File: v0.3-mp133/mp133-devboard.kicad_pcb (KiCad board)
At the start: 4 copper layers, 39.9 x 57.9 mm, 122 parts, among them CON1 microSDCon_SMT_104031-0811, J1 Pins_02x40_P0.4mm_W3.0mm_SMT, J2 Pins_02x40_P0.4mm_W3.0mm_SMT, J3 USB-C_Receptacle_Molex_217179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, J4 Pins_02x04_RightAngle_P2.54mm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, J5 Conn_01x02, J6 Pins_02x05_P1.27mm_SMT, U13 NCP51460SN33, U14 DDR3L-RAM-4Gb_MT41K256M16TW, U15 AP6230xZ6, U16 AP6230xZ6, U17 AP6230xZ6, U18 TAR5S33, U19 TAR5S33, U2 STM32MP15xxAD, U20 AP2411SN, U3 USBLC6-2SC6, U5 NORFLASH_W25Q128JV, X1 24MHz_8pF_2x1.6mm

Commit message: Work on mp133 devboard PCB
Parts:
- removed C50, C51, C52, C53, C54, C55, C59, C60, C62, C63, C70, C73, C79: 1uF_0402_25V, 4ms_Capacitor:C_0402
- removed C61, C64, C82, C87, C93, C95: 100nF_0402_16V, 4ms_Capacitor:C_0402
- removed C71, C74, C80: 3.3nF_0402_16V, 4ms_Capacitor:C_0402
- removed R41: 10k_0402, 4ms_Resistor:R_0402
- removed X1: 24MHz_8pF_2x1.6mm, 4ms_Crystal:Crystal_2.0x1.6mm_4pin
- added C102: 100nF_0402_16V, 4ms_Capacitor:C_0402, B.Cu at (254.1, 59.8)
- added C103: 100nF_0402_16V, 4ms_Capacitor:C_0402, B.Cu at (243.6, 65.3)
- added C106: 100nF_0402_16V, 4ms_Capacitor:C_0402, B.Cu at (244.0, 55.9)
- added C110: 6.8pF_0402_25V, 4ms_Capacitor:C_0402, F.Cu at (251.5, 85.8)
- added C110: 6.8pF_0402_25V, 4ms_Capacitor:C_0402, F.Cu at (142.8, 74.5)
- added C111: 6.8pF_0402_25V, 4ms_Capacitor:C_0402, F.Cu at (142.8, 76.5)
- added C111: 6.8pF_0402_25V, 4ms_Capacitor:C_0402, F.Cu at (253.6, 84.1)
- added C13: 1uF_0402_25V, 4ms_Capacitor:C_0402, B.Cu at (250.9, 72.1)
- added C174: 1uF_0201_4V, 4ms_Capacitor:C_0201, F.Cu at (142.5, 64.2)
- added C174: 1uF_0201_4V, 4ms_Capacitor:C_0201, B.Cu at (245.1, 79.1)
- added C175: 1nF_0201_4V, 4ms_Capacitor:C_0201, F.Cu at (142.5, 65.9)
- added C175: 1nF_0201_4V, 4ms_Capacitor:C_0201, B.Cu at (245.1, 74.7)
- added C176: 1uF_0201_4V, 4ms_Capacitor:C_0201, F.Cu at (142.5, 67.6)
- added C176: 1uF_0201_4V, 4ms_Capacitor:C_0201, B.Cu at (245.2, 76.5)
- added C177: 1uF_0201_4V, 4ms_Capacitor:C_0201, F.Cu at (142.5, 69.3)
- added C177: 1uF_0201_4V, 4ms_Capacitor:C_0201, B.Cu at (245.2, 77.7)
- added C182: 1uF_0201_4V, 4ms_Capacitor:C_0201, F.Cu at (142.5, 71.0)
- added C182: 1uF_0201_4V, 4ms_Capacitor:C_0201, B.Cu at (249.3, 55.0)
- added C183: 1uF_0201_4V, 4ms_Capacitor:C_0201, F.Cu at (142.5, 72.6)
- added C183: 1uF_0201_4V, 4ms_Capacitor:C_0201, B.Cu at (246.1, 80.0)
- added C184: 1nF_0201_4V, 4ms_Capacitor:C_0201, F.Cu at (144.7, 64.2)
- added C184: 1nF_0201_4V, 4ms_Capacitor:C_0201, B.Cu at (246.2, 74.9)
- added C185: 1uF_0201_4V, 4ms_Capacitor:C_0201, F.Cu at (144.7, 65.9)
- added C185: 1uF_0201_4V, 4ms_Capacitor:C_0201, B.Cu at (246.2, 76.1)
- added C186: 1uF_0201_4V, 4ms_Capacitor:C_0201, F.Cu at (144.7, 67.6)
- added C186: 1uF_0201_4V, 4ms_Capacitor:C_0201, B.Cu at (246.2, 77.6)
- added C187: 1uF_0201_4V, 4ms_Capacitor:C_0201, F.Cu at (144.7, 69.3)
- added C187: 1uF_0201_4V, 4ms_Capacitor:C_0201, B.Cu at (246.2, 78.8)
- added C188: 1uF_0201_4V, 4ms_Capacitor:C_0201, F.Cu at (144.7, 71.0)
- added C188: 1uF_0201_4V, 4ms_Capacitor:C_0201, B.Cu at (247.3, 75.8)
- added C189: 1uF_0201_4V, 4ms_Capacitor:C_0201, F.Cu at (144.7, 72.6)
- added C189: 1uF_0201_4V, 4ms_Capacitor:C_0201, B.Cu at (247.2, 76.8)
- added C190: 1uF_0201_4V, 4ms_Capacitor:C_0201, F.Cu at (147.0, 64.2)
- added C190: 1uF_0201_4V, 4ms_Capacitor:C_0201, B.Cu at (247.3, 77.9)
- added C191: 1uF_0201_4V, 4ms_Capacitor:C_0201, F.Cu at (147.0, 65.9)
- added C191: 1uF_0201_4V, 4ms_Capacitor:C_0201, B.Cu at (247.6, 80.0)
- added C192: 1nF_0201_4V, 4ms_Capacitor:C_0201, F.Cu at (147.0, 67.6)
- added C192: 1nF_0201_4V, 4ms_Capacitor:C_0201, B.Cu at (247.6, 56.9)
- added C193: 1nF_0201_4V, 4ms_Capacitor:C_0201, F.Cu at (147.0, 69.3)
- added C193: 1nF_0201_4V, 4ms_Capacitor:C_0201, B.Cu at (247.7, 74.9)
- added C194: 1uF_0201_4V, 4ms_Capacitor:C_0201, F.Cu at (147.0, 71.0)
- added C194: 1uF_0201_4V, 4ms_Capacitor:C_0201, B.Cu at (247.7, 78.9)
- added C195: 1uF_0201_4V, 4ms_Capacitor:C_0201, F.Cu at (147.0, 72.6)
- added C195: 1uF_0201_4V, 4ms_Capacitor:C_0201, B.Cu at (248.2, 76.1)
- added C196: 1uF_0201_4V, 4ms_Capacitor:C_0201, F.Cu at (149.2, 64.2)
- added C196: 1uF_0201_4V, 4ms_Capacitor:C_0201, B.Cu at (248.2, 77.6)
- added C197: 1uF_0201_4V, 4ms_Capacitor:C_0201, F.Cu at (149.2, 65.9)
- added C197: 1uF_0201_4V, 4ms_Capacitor:C_0201, B.Cu at (248.9, 80.0)
- added C198: 1uF_0201_4V, 4ms_Capacitor:C_0201, F.Cu at (149.2, 67.6)
- added C198: 1uF_0201_4V, 4ms_Capacitor:C_0201, B.Cu at (250.2, 74.8)
- added C199: 1uF_0201_4V, 4ms_Capacitor:C_0201, F.Cu at (149.2, 69.3)
- added C199: 1uF_0201_4V, 4ms_Capacitor:C_0201, B.Cu at (249.0, 74.9)
- added C200: 1uF_0201_4V, 4ms_Capacitor:C_0201, F.Cu at (149.2, 71.0)
- added C200: 1uF_0201_4V, 4ms_Capacitor:C_0201, B.Cu at (249.2, 75.9)
- added C201: 1uF_0201_4V, 4ms_Capacitor:C_0201, F.Cu at (149.2, 72.6)
- added C201: 1uF_0201_4V, 4ms_Capacitor:C_0201, B.Cu at (248.9, 78.9)
- added C202: 1uF_0201_4V, 4ms_Capacitor:C_0201, F.Cu at (151.5, 64.2)
- added C202: 1uF_0201_4V, 4ms_Capacitor:C_0201, B.Cu at (249.2, 77.9)
- added C203: 1uF_0201_4V, 4ms_Capacitor:C_0201, F.Cu at (151.5, 65.9)
- added C203: 1uF_0201_4V, 4ms_Capacitor:C_0201, B.Cu at (249.1, 77.0)
- added C204: 1nF_0201_4V, 4ms_Capacitor:C_0201, F.Cu at (151.5, 67.6)
- added C204: 1nF_0201_4V, 4ms_Capacitor:C_0201, B.Cu at (250.3, 73.9)
- added C205: 1uF_0201_4V, 4ms_Capacitor:C_0201, F.Cu at (151.5, 69.3)
- added C205: 1uF_0201_4V, 4ms_Capacitor:C_0201, B.Cu at (250.1, 78.8)
- added C206: 1nF_0201_4V, 4ms_Capacitor:C_0201, F.Cu at (151.5, 71.0)
- added C206: 1nF_0201_4V, 4ms_Capacitor:C_0201, B.Cu at (248.5, 73.9)
- added C207: 1uF_0201_4V, 4ms_Capacitor:C_0201, F.Cu at (151.5, 72.6)
- added C207: 1uF_0201_4V, 4ms_Capacitor:C_0201, B.Cu at (250.4, 79.9)
- added C208: 1uF_0201_4V, 4ms_Capacitor:C_0201, F.Cu at (153.7, 64.2)
- added C208: 1uF_0201_4V, 4ms_Capacitor:C_0201, B.Cu at (250.3, 76.6)
- added C209: 1uF_0201_4V, 4ms_Capacitor:C_0201, F.Cu at (153.7, 65.9)
- added C209: 1uF_0201_4V, 4ms_Capacitor:C_0201, B.Cu at (250.3, 77.8)
- added C211: 1nF_0201_4V, 4ms_Capacitor:C_0201, F.Cu at (153.7, 67.6)
- added C211: 1nF_0201_4V, 4ms_Capacitor:C_0201, B.Cu at (251.2, 74.2)
- added C212: 1uF_0201_4V, 4ms_Capacitor:C_0201, F.Cu at (153.7, 69.3)
- added C212: 1uF_0201_4V, 4ms_Capacitor:C_0201, B.Cu at (251.2, 75.5)
- added C213: 1uF_0201_4V, 4ms_Capacitor:C_0201, F.Cu at (153.7, 71.0)
- added C213: 1uF_0201_4V, 4ms_Capacitor:C_0201, B.Cu at (251.2, 76.7)
- added C215: 1uF_0201_4V, 4ms_Capacitor:C_0201, F.Cu at (153.7, 72.6)
- added C215: 1uF_0201_4V, 4ms_Capacitor:C_0201, B.Cu at (251.4, 79.3)
- added C29: 2.2uF_0402_6.3V, 4ms_Capacitor:C_0402, B.Cu at (252.5, 76.7)
- added C30: 100nF_0402_16V, 4ms_Capacitor:C_0402, B.Cu at (253.0, 79.9)
- added C31: 1uF_0402_25V, 4ms_Capacitor:C_0402, B.Cu at (252.9, 78.9)
- added C32: 2.2uF_0402_6.3V, 4ms_Capacitor:C_0402, B.Cu at (254.2, 75.3)
- added C33: 1uF_0402_25V, 4ms_Capacitor:C_0402, B.Cu at (252.4, 81.0)
- added C42: 100nF_0402_16V, 4ms_Capacitor:C_0402, B.Cu at (253.4, 64.2)
- added C43: 100nF_0402_16V, 4ms_Capacitor:C_0402, B.Cu at (243.6, 60.1)
- added C72: 100nF_0402_50V, 4ms_Capacitor:C_0402, B.Cu at (254.6, 81.9)
- added C81: 10uF_0603_10V, 4ms_Capacitor:C_0603, F.Cu at (254.2, 56.8)
- added C83: 10uF_0603_10V, 4ms_Capacitor:C_0603, B.Cu at (242.7, 55.8)
- added C84: 4.7uF_0402_6.3V, 4ms_Capacitor:C_0402, B.Cu at (254.6, 79.8)
- added C92: 100nF_0402_16V, 4ms_Capacitor:C_0402, B.Cu at (243.6, 59.1)
- added C94: 100nF_0402_16V, 4ms_Capacitor:C_0402, B.Cu at (251.6, 57.4)
- added C98: 100nF_0402_16V, 4ms_Capacitor:C_0402, F.Cu at (253.9, 66.5)
- added C99: 100nF_0402_16V, 4ms_Capacitor:C_0402, F.Cu at (255.5, 56.9)
- added D11: BAT54LP, 4ms_Diode:DFN-1006-2, F.Cu at (256.1, 72.9)
- added D26: BAT54LP, 4ms_Diode:DFN-1006-2, F.Cu at (255.7, 71.5)
- added D26: BAT54LP, 4ms_Diode:DFN-1006-2, F.Cu at (145.8, 78.3)
- added L4: 1uH_3.2A_2520, Inductor_SMD:L_1008_2520Metric, F.Cu at (146.7, 75.4)
- added R30: 10k_0402, 4ms_Resistor:R_0402, B.Cu at (250.9, 84.9)
- added R52: 240Ω_0402, 4ms_Resistor:R_0402, B.Cu at (253.9, 73.7)
- added R59: 240Ω_0402, 4ms_Resistor:R_0402, B.Cu at (253.4, 63.0)
- added R67: 10k_0402, 4ms_Resistor:R_0402, B.Cu at (253.4, 62.0)
- added R68: 100Ω_0402, 4ms_Resistor:R_0402, B.Cu at (249.6, 61.4)
- added R69: 10k_0402, 4ms_Resistor:R_0402, B.Cu at (242.8, 73.9)
- added R76: 10k_0402, 4ms_Resistor:R_0402, F.Cu at (139.9, 64.3)
- added R76: 10k_0402, 4ms_Resistor:R_0402, F.Cu at (255.1, 73.0)
- added R77: 10k_0402, 4ms_Resistor:R_0402, F.Cu at (254.8, 70.0)
- added R77: 10k_0402, 4ms_Resistor:R_0402, F.Cu at (139.9, 66.3)
- added R78: 1k_0402, 4ms_Resistor:R_0402, F.Cu at (139.9, 68.3)
- added R78: 1k_0402, 4ms_Resistor:R_0402, B.Cu at (252.8, 72.1)
- added R79: 1k_0402, 4ms_Resistor:R_0402, F.Cu at (139.9, 70.3)
- added R79: 1k_0402, 4ms_Resistor:R_0402, B.Cu at (251.9, 72.1)
- added R80: 10k_0402, 4ms_Resistor:R_0402, F.Cu at (139.9, 72.3)
- added R81: 14.7k_0402, 4ms_Resistor:R_0402, F.Cu at (139.9, 74.3)
- added U14: DDR3L-RAM-4Gb_MT41K256M16TW, 4ms_Package_QFP:FBGA-96_Layout2x3x16_Body8x14_P0.8mm, F.Cu at (248.4, 61.5)
- added U2: STM32MP131DAF7, 4ms_Package_QFP:TFBGA-320_11x11mm_P0.5, F.Cu at (248.2, 76.9)
- added U21: AP6230xZ6, 4ms_Package_SOT:SOT-563, F.Cu at (151.2, 78.5)
- added X2: 24MHz_8pF_2x1.6mm, 4ms_Crystal:Crystal_2.0x1.6mm_4pin, F.Cu at (151.2, 75.1)
- added X2: 24MHz_8pF_2x1.6mm, 4ms_Crystal:Crystal_2.0x1.6mm_4pin, F.Cu at (251.8, 84.2)
- C13: value 6.8pF_0402_25V -> 1uF_0402_25V
- C14: value 6.8pF_0402_25V -> 2.2uF_0603_25V; footprint 4ms_Capacitor:C_0402 -> 4ms_Capacitor:C_0603
- C24: value 10nF_0402_16V -> 100nF_0402_16V
- C40: value 100nF_0402_16V -> 22uF_0603_6.3V; footprint 4ms_Capacitor:C_0402 -> 4ms_Capacitor:C_0603
- R62: value 20k_0402 -> 17.4k_0402
- U2: value STM32MP15xxAD -> STM32MP133DAF
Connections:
- C13 pad 2: Net-(U2B-PH0-OSC_IN) -> VREF_DDR
- C14 pad 2: Net-(U2B-PH1-OSC_OUT) -> +12V
- C24 pad 1: GND -> Net-(U21-SW)
- C24 pad 2: /NRST_CORE -> Net-(U21-BST)
- C29 pad 2: Net-(U2D-VDDA1V1_REG) -> Net-(U2E-VDDA1V1_REG)
- C40 pad 2: VREF_DDR -> VDD_CPU
- J1 pad 1: /PD3 -> Net-(J1-Pin_1)
- J1 pad 11: /PE4 -> /PB9
- J1 pad 12: /PE4 -> /PB9
- J1 pad 2: /PD3 -> Net-(J1-Pin_1)
- J1 pad 3: /PA8 -> Net-(J1-Pin_3)
- J1 pad 39: /PC7 -> Net-(J1-Pin_39)
- J1 pad 4: /PA8 -> Net-(J1-Pin_3)
- J1 pad 40: /PC7 -> Net-(J1-Pin_39)
- J1 pad 41: /PA10 -> Net-(J1-Pin_41)
- J1 pad 42: /PA10 -> Net-(J1-Pin_41)
- J1 pad 43: /PE0 -> /PD0
- J1 pad 44: /PE0 -> /PD0
- J1 pad 45: /PD12 -> /PE11
- J1 pad 46: /PD12 -> /PE11
- J1 pad 47: /PD13 -> /PH12
- J1 pad 48: /PD13 -> /PH12
- J1 pad 49: /PD11 -> /PD6
- J1 pad 5: /PB9 -> Net-(J1-Pin_5)
- J1 pad 50: /PD11 -> /PD6
- J1 pad 55: /PB10 -> Net-(J1-Pin_55)
- J1 pad 56: /PB10 -> Net-(J1-Pin_55)
- J1 pad 57: /PG9 -> Net-(J1-Pin_57)
- J1 pad 58: /PG9 -> Net-(J1-Pin_57)
- J1 pad 59: /PA12 -> /PE8
- J1 pad 6: /PB9 -> Net-(J1-Pin_5)
- J1 pad 60: /PA12 -> /PE8
- J1 pad 61: /PA11 -> /PD12
- J1 pad 62: /PA11 -> /PD12
- J1 pad 63: /PE10 -> Net-(J1-Pin_63)
- J1 pad 64: /PE10 -> Net-(J1-Pin_63)
- J2 pad 1: /PE3 -> Net-(J2-Pin_1)
- J2 pad 10: /PB7 -> /PD7
- J2 pad 11: /PE11 -> /PH11
- J2 pad 12: /PE11 -> /PH11
- J2 pad 13: /PC6 -> Net-(J2-Pin_13)
- J2 pad 14: /PC6 -> Net-(J2-Pin_13)
- J2 pad 15: /PE6 -> /PA8
- J2 pad 16: /PE6 -> /PA8
- J2 pad 17: /PG15 -> Net-(J2-Pin_17)
- J2 pad 18: /PG15 -> Net-(J2-Pin_17)
- J2 pad 19: /PE12 -> /PH6
- J2 pad 2: /PE3 -> Net-(J2-Pin_1)
- J2 pad 20: /PE12 -> /PH6
- J2 pad 21: /PE13 -> /PG1
- J2 pad 22: /PE13 -> /PG1
- J2 pad 3: /PD10 -> Net-(J2-Pin_3)
- J2 pad 31: /PA3 -> /PA1
- J2 pad 32: /PA3 -> /PA1
- J2 pad 33: /PC3 -> /PA2
- J2 pad 34: /PC3 -> /PA2
- J2 pad 35: /PC2 -> Net-(J2-Pin_35)
- J2 pad 36: /PC2 -> Net-(J2-Pin_35)
- J2 pad 37: /PC1 -> /PA4
- J2 pad 38: /PC1 -> /PA4
- J2 pad 39: /PA1 -> /PA5
- J2 pad 4: /PD10 -> Net-(J2-Pin_3)
- J2 pad 40: /PA1 -> /PA5
- J2 pad 41: /PB0 -> /PC0
- J2 pad 42: /PB0 -> /PC0
- J2 pad 43: /PA2 -> /PA7
- J2 pad 44: /PA2 -> /PA7
- J2 pad 45: /PB1 -> /PC1
- J2 pad 46: /PB1 -> /PC1
- J2 pad 47: /PC5 -> /PC2
- J2 pad 48: /PC5 -> /PC2
- J2 pad 5: /PB4 -> Net-(J2-Pin_5)
- J2 pad 51: /PC0 -> /PC5
- J2 pad 52: /PC0 -> /PC5
- J2 pad 53: /PA7 -> /PA3
- J2 pad 54: /PA7 -> /PA3
- J2 pad 55: /PA5 -> /PC3
- J2 pad 56: /PA5 -> /PC3
- J2 pad 59: /PA4 -> /PF12
- J2 pad 6: /PB4 -> Net-(J2-Pin_5)
- J2 pad 60: /PA4 -> /PF12
- J2 pad 61: /PF11 -> /PB0
- J2 pad 62: /PF11 -> /PB0
- J2 pad 69: /PE2 -> Net-(J2-Pin_69)
- J2 pad 7: /PG6 -> Net-(J2-Pin_7)
- J2 pad 70: /PE2 -> Net-(J2-Pin_69)
- J2 pad 71: /PG13 -> Net-(J2-Pin_71)
- J2 pad 72: /PG13 -> Net-(J2-Pin_71)
- J2 pad 73: /PB8 -> /PH3
- J2 pad 74: /PB8 -> /PH3
- J2 pad 75: /PB2 -> Net-(J2-Pin_75)
- J2 pad 76: /PB2 -> Net-(J2-Pin_75)
- J2 pad 8: /PG6 -> Net-(J2-Pin_7)
- J2 pad 9: /PB7 -> /PD7
- JP2 pad 1: /PB14 -> /DEBUG3
- JP3 pad 3: /PB15 -> /DEBUG2
- R52 pad 1: Net-(U2E-DDR_ZQ) -> Net-(U2C-DDR_ZQ)
- U14 pad A2: /DDR_DQ7 -> /DDR_DQ5
- U14 pad A7: /DDR_DQ2 -> /DDR_DQ0
- U14 pad B8: /DDR_DQ4 -> /DDR_DQ1
- U14 pad C2: /DDR_DQ1 -> /DDR_DQ6
- U14 pad C3: /DDR_DQ0 -> /DDR_DQ7
- U14 pad C8: /DDR_DQ5 -> /DDR_DQ4
- U14 pad D7: /DDR_DQ6 -> /DDR_DQ2
- U14 pad E3: /DDR_DQ9 -> /DDR_DQ8
- U14 pad F2: /DDR_DQ8 -> /DDR_DQ13
- U14 pad F7: /DDR_DQ11 -> /DDR_DQ15
- U14 pad F8: /DDR_DQ15 -> /DDR_DQ12
- U14 pad H3: /DDR_DQ13 -> /DDR_DQ9
- U14 pad H8: /DDR_DQ12 -> /DDR_DQ11
- U2 pad 1A1: unconnected-(U2B-PE1-Pad1A1) -> (no net)
- U2 pad 1A2: /PD10 -> (no net)
- U2 pad 1A3: /PE3 -> (no net)
- U2 pad 1A4: /PB14 -> (no net)
- U2 pad 1A5: /PD2 -> (no net)
- U2 pad 1A6: GND -> (no net)
- U2 pad 1A7: unconnected-(U2D-VDD1V2_DSI_REG-Pad1A7) -> (no net)
- U2 pad 1A8: Net-(U2E-DDR_ZQ) -> (no net)
- U2 pad 1A9: /DDR_A7 -> (no net)
- U2 pad 1B1: unconnected-(U2A-PD6-Pad1B1) -> (no net)
- U2 pad 1B2: unconnected-(U2B-PE14-Pad1B2) -> (no net)
- U2 pad 1B3: VDD_CORE -> (no net)
- U2 pad 1B4: /PC12 -> (no net)
- U2 pad 1B5: VDD_CORE -> (no net)
- U2 pad 1B6: unconnected-(U2D-VDDA1V8_DSI-Pad1B6) -> (no net)
- U2 pad 1B7: unconnected-(U2D-VDD1V2_DSI_PHY-Pad1B7) -> (no net)
- U2 pad 1B8: GND -> (no net)
- U2 pad 1B9: VDD_DDR -> (no net)
- U2 pad 1C1: unconnected-(U2A-PD9-Pad1C1) -> (no net)
- U2 pad 1C2: unconnected-(U2A-PD15-Pad1C2) -> (no net)
- U2 pad 1C3: GND -> (no net)
- U2 pad 1C4: VDD_CORE -> (no net)
- U2 pad 1C5: GND -> (no net)
- U2 pad 1C6: VDD_CORE -> (no net)
- U2 pad 1C7: GND -> (no net)
- U2 pad 1C8: unconnected-(U2E-DDR_DTO1-Pad1C8) -> (no net)
- U2 pad 1C9: /DDR_A5 -> (no net)
- U2 pad 1D1: VDD -> (no net)
- U2 pad 1D2: GND -> (no net)
- U2 pad 1D3: VDD_CORE -> (no net)
- U2 pad 1D4: GND -> (no net)
- U2 pad 1D5: VDD_CORE -> (no net)
- U2 pad 1D6: GND -> (no net)
- U2 pad 1D7: VDD_CORE -> (no net)
- U2 pad 1D8: unconnected-(U2E-DDR_DTO0-Pad1D8) -> (no net)
- U2 pad 1D9: VDD_DDR -> (no net)
- U2 pad 1E1: unconnected-(U2A-PD14-Pad1E1) -> (no net)
- U2 pad 1E2: VDD -> (no net)
- U2 pad 1E3: GND -> (no net)
- U2 pad 1E4: VDD_CORE -> (no net)
- U2 pad 1E5: GND -> (no net)
- U2 pad 1E6: VDD_CORE -> (no net)
- U2 pad 1E7: GND -> (no net)
- U2 pad 1E8: VDD_CORE -> (no net)
- U2 pad 1E9: /DDR_RASN -> (no net)
- U2 pad 1F1: VDDA -> (no net)
- U2 pad 1F2: VDDA -> (no net)
- U2 pad 1F3: VDD -> (no net)
- U2 pad 1F4: GND -> (no net)
- U2 pad 1F5: VDD_CORE -> (no net)
- U2 pad 1F6: GND -> (no net)
- U2 pad 1F7: VDD_CORE -> (no net)
- U2 pad 1F8: unconnected-(U2E-DDR_ATO-Pad1F8) -> (no net)
- U2 pad 1F9: VDD_DDR -> (no net)
- U2 pad 1G1: GNDADC -> (no net)
- U2 pad 1G2: GND -> (no net)
- U2 pad 1G3: VDD -> (no net)
- U2 pad 1G4: VDD -> (no net)
- U2 pad 1G5: GND -> (no net)
- U2 pad 1G6: VDD_CORE -> (no net)
- U2 pad 1G7: GND -> (no net)
- U2 pad 1G8: VDD_CORE -> (no net)
- U2 pad 1G9: /DDR_A6 -> (no net)
- U2 pad 1H1: /PA5 -> (no net)
- U2 pad 1H2: GND -> (no net)
- U2 pad 1H3: GND -> (no net)
- U2 pad 1H4: GND -> (no net)
- U2 pad 1H5: VDDA_1V8 -> (no net)
- U2 pad 1H6: GND -> (no net)
- U2 pad 1H7: VDD_USB -> (no net)
- U2 pad 1H8: GND -> (no net)
- U2 pad 1H9: VDD_DDR -> (no net)
- U2 pad 1J1: /PA4 -> (no net)
- U2 pad 1J2: unconnected-(U2A-PB13-Pad1J2) -> (no net)
- U2 pad 1J3: VDD -> (no net)
- U2 pad 1J4: unconnected-(U2B-PE9-Pad1J4) -> (no net)
- U2 pad 1J5: GND -> (no net)
- U2 pad 1J6: Net-(U2D-VDDA1V1_REG) -> (no net)
- U2 pad 1J7: /FLASH_CLK -> (no net)
- U2 pad 1J8: /USB_RREF -> (no net)
- U2 pad 1J9: GND -> (no net)
- U2 pad A10: /PE4 -> unconnected-(U2B-PG7-PadA10)
- U2 pad A15: /JTDO_SWO -> /PB9
- U2 pad A16: /JTCK_SWCLK -> unconnected-(U2B-PF0-PadA16)
- U2 pad A17: /DDR_DQ0 -> (no net)
- U2 pad A18: /DDR_DQ1 -> /PC10
- U2 pad A19: GND -> /PC12
- U2 pad A3: /PB7 -> /PE13
- U2 pad A4: /PC6 -> /PE12
- U2 pad A6: GND -> /PD12
- U2 pad A7: /PD3 -> /PG0
- U2 pad A9: /PC8 -> unconnected-(U2B-PE15-PadA9)
- U2 pad B1: /PG15 -> /PD0
- U2 pad B10: /PC10 -> /PG4
- U2 pad B12: unconnected-(U2C-DSI_CKN-PadB12) -> GND
- U2 pad B14: /JTRST -> /PC6
- U2 pad B15: /JTDI -> unconnected-(U2A-PB15-PadB15)
- U2 pad B16: /DDR_DQ3 -> unconnected-(U2A-PB14-PadB16)
- U2 pad B17: /DDR_DQ7 -> /PE3
- U2 pad B18: /DDR_DQS0_N -> /PC11
- U2 pad B19: /DDR_DQS0_P -> /DDR_DQ4
- U2 pad B2: /PE6 -> /PE11
- U2 pad B3: /DEBUG0 -> unconnected-(U2B-PF5-PadB3)
- U2 pad B4: unconnected-(U2A-PA15-PadB4) -> /UART_RX
- U2 pad B5: /PG6 -> unconnected-(U2A-PD8-PadB5)
- U2 pad B6: /PB4 -> /PE0
- U2 pad B7: /DEBUG1 -> unconnected-(U2B-PE9-PadB7)
- U2 pad B8: /PA8 -> unconnected-(U2B-PH14-PadB8)
- U2 pad B9: /PC9 -> /PE8
- U2 pad C1: /PE12 -> unconnected-(U2A-PB6-PadC1)
- U2 pad C10: /PC7 -> /PE10
- U2 pad C11: /PC11 -> unconnected-(U2A-PB12-PadC11)
- U2 pad C13: unconnected-(U2D-VDD_DSI-PadC13) -> /PC7
- U2 pad C14: GND -> /DEBUG0
- U2 pad C15: /JTMS_SWDIO -> VDD
- U2 pad C16: /DDR_RESETN -> /DEBUG1
- U2 pad C17: /DDR_DQM0 -> /PG6
- U2 pad C18: /DDR_DQ2 -> /PC8
- U2 pad C19: /DDR_DQ6 -> /PD2
- U2 pad C2: /PE0 -> /PD3
- U2 pad C5: /UART_RX -> unconnected-(U2A-PD1-PadC5)
- U2 pad C6: unconnected-(U2A-PA9-PadC6) -> /PB7
- U2 pad C8: /PB15 -> unconnected-(U2A-PD5-PadC8)
- U2 pad C9: /PB9 -> unconnected-(U2A-PD9-PadC9)
- U2 pad D1: unconnected-(U2B-PG12-PadD1) -> /PB8
- U2 pad D17: GND -> (no net)
- U2 pad D18: /DDR_DQ4 -> (no net)
- U2 pad D19: /DDR_DQ5 -> /DDR_DQ2
- U2 pad D2: /PE11 -> /PD6
- U2 pad D3: unconnected-(U2B-PE15-PadD3) -> /PH12
- U2 pad E1: /DFU_BOOT -> (no net)
- U2 pad E17: /DDR_A13 -> VDD
- U2 pad E18: /DDR_A9 -> (no net)
- U2 pad E2: /NRST -> unconnected-(U2B-PH2-PadE2)
- U2 pad E3: /PE13 -> unconnected-(U2B-PH8-PadE3)
- U2 pad F17: /DDR_A2 -> GND
- U2 pad F19: /DDR_A3 -> /DDR_DQ7
- U2 pad F2: unconnected-(U2A-PC15-OSC32_OUT-PadF2) -> /PG9
- U2 pad F3: GND -> /PD11
- U2 pad G1: GND -> /FLASH_IO2
- U2 pad G17: GND -> VDD_DDR
- U2 pad G18: /DDR_A0 -> (no net)
- U2 pad G19: /DDR_BA0 -> /DDR_A13
- U2 pad G2: unconnected-(U2A-PC14-OSC32_IN-PadG2) -> /PG10
- U2 pad G3: unconnected-(U2A-PC13-PadG3) -> /PG5
- U2 pad H1: /BOOT2 -> (no net)
- U2 pad H17: /DDR_BA2 -> /DDR_RESETN
- U2 pad H18: /DDR_ODT -> /DDR_BA2
- U2 pad H2: Net-(U2B-PH0-OSC_IN) -> /PE4
- U2 pad H3: /BOOT0 -> /FLASH_CLK
- U2 pad J17: /DDR_CSN -> /DDR_A7
- U2 pad J18: /DDR_WEN -> (no net)
- U2 pad J19: /DDR_CASN -> /DDR_BA0
- U2 pad J2: Net-(U2B-PH1-OSC_OUT) -> /PD13
- U2 pad J3: /NRST_CORE -> /FLASH_CS
- U2 pad K1: unconnected-(U2C-PWR_LP-PadK1) -> GND
- U2 pad K17: GND -> VDD_DDR
- U2 pad K18: /DDR_CLK_N -> (no net)
- U2 pad K19: GND -> /DDR_WEN
- U2 pad K3: GND -> / PH11
- U2 pad L1: unconnected-(U2A-PA14-PadL1) -> (no net)
- U2 pad L17: /DDR_CLK_P -> GND
- U2 pad L18: unconnected-(U2E-DDR_A15-PadL18) -> /DDR_A10
- U2 pad L2: unconnected-(U2A-PA13-PadL2) -> VDD
- U2 pad L3: VDD -> unconnected-(U2A-PC15-OSC32_OUT-PadL3)
- U2 pad M17: /DDR_A10 -> VDD_DDR
- U2 pad M18: /DDR_A12 -> (no net)
- U2 pad M19: /DDR_A1 -> /DDR_A12
- U2 pad M2: /PWR_ON -> unconnected-(U2A-PC14-OSC32_IN-PadM2)
- U2 pad M3: VREF+ -> unconnected-(U2A-PC13-PadM3)
- U2 pad N1: GND -> /PE2
- U2 pad N17: GND -> /DDR_A11
- U2 pad N18: /DDR_A14 -> (no net)
- U2 pad N19: /DDR_A11 -> /DDR_A14
- U2 pad N2: /PA3 -> unconnected-(U2B-PF4-PadN2)
- U2 pad N3: /PA0 -> unconnected-(U2B-PH6-PadN3)
- U2 pad P1: /PE2 -> (no net)
- U2 pad P17: /DDR_CKE -> unconnected-(U2C-DDR_DTO1-PadP17)
- U2 pad P18: /DDR_BA1 -> unconnected-(U2C-DDR_ATO-PadP18)
- U2 pad P2: /PC2 -> /PA8
- U2 pad P3: /PC3 -> unconnected-(U2B-PF7-PadP3)
- U2 pad R17: /DDR_A4 -> VDD_DDR
- U2 pad R18: /DDR_DQ8 -> (no net)
- U2 pad R19: GND -> /DDR_A4
- U2 pad R3: /PG13 -> /PH3
- U2 pad T1: /PA1 -> GND
- U2 pad T17: /DDR_A8 -> GND
- U2 pad T18: /DDR_DQ13 -> VREF_DDR
- U2 pad T2: /PC1 -> /PE6
- U2 pad T3: /PA2 -> Net-(U2B-PH0-OSC_IN)
- U2 pad U1: /PB1 -> (no net)
- U2 pad U10: /FLASH_IO3 -> /PA6
- U2 pad U12: unconnected-(U2B-PE8-PadU12) -> VDD_CORE
- U2 pad U13: /PD13 -> GND
- U2 pad U14: /PD12 -> VDD_CORE
- U2 pad U15: /PA11 -> VDD_DDR
- U2 pad U16: /PA10 -> GND
- U2 pad U17: /DDR_DQ14 -> /PWR_ON
- U2 pad U18: /DDR_DQS1_N -> (no net)
- U2 pad U19: /DDR_DQ9 -> /DDR_DQ13
- U2 pad U2: /PB0 -> Net-(U2B-PH1-OSC_OUT)
- U2 pad U3: unconnected-(U2A-PB11-PadU3) -> GNDADC
- U2 pad U4: /PC0 -> (no net)
- U2 pad U5: /PB10 -> GND
- U2 pad U6: unconnected-(U2B-PG11-PadU6) -> GND
- U2 pad U7: /PG10 -> VDD
- U2 pad U8: /PD11 -> VDDA
- U2 pad U9: GND -> GNDADC
- U2 pad V1: /PC5 -> /PD7
- U2 pad V10: /USB_HS_DP -> (no net)
- U2 pad V11: unconnected-(U2B-PG7-PadV11) -> /JTRST
- U2 pad V12: /PE10 -> (no net)
- U2 pad V13: /PB2 -> (no net)
- U2 pad V14: unconnected-(U2A-USB_DP1-PadV14) -> Net-(U2E-VDDA1V1_REG)
- U2 pad V15: /PA12 -> (no net)
- U2 pad V16: /USB_VBUS -> GND
- U2 pad V17: /DDR_DQ15 -> (no net)
- U2 pad V18: /DDR_DQM1 -> (no net)
- U2 pad V19: /DDR_DQS1_P -> unconnected-(U2D-PWR_LP-PadV19)
- U2 pad V2: /PC4 -> VDD
- U2 pad V3: unconnected-(U2A-PB12-PadV3) -> /PG2
- U2 pad V4: /PB8 -> (no net)
- U2 pad V5: unconnected-(U2A-PB5-PadV5) -> (no net)
- U2 pad V6: unconnected-(U2B-PG8-PadV6) -> /PA7
- U2 pad V7: unconnected-(U2B-PE7-PadV7) -> (no net)
- U2 pad V8: /FLASH_IO0 -> GNDADC
- U2 pad V9: /FLASH_IO1 -> (no net)
- U2 pad W1: GND -> /PG3
- U2 pad W10: /USB_HS_DM -> /DEBUG1
- U2 pad W11: /FLASH_CS -> VDD
- U2 pad W13: GND -> unconnected-(U2A-PA14-PadW13)
- U2 pad W14: unconnected-(U2A-USB_DM1-PadW14) -> VDD_USB
- U2 pad W16: VREF_DDR -> GND
- U2 pad W17: /DDR_DQ12 -> GND
- U2 pad W18: /DDR_DQ11 -> /JTDO_SWO
- U2 pad W19: GND -> /DDR_DQ12
- U2 pad W2: /PA7 -> /PG12
- U2 pad W3: /PA6 -> Net-(U2D-PWR_CPU_ON)
- U2 pad W4: /PF11 -> /PF13
- U2 pad W5: GND -> /PC0
- U2 pad W7: /FLASH_IO2 -> VREF+
- U2 pad W8: /PG9 -> /PB0
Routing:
- net GND: track 266.9 -> 442.7 mm, vias 90 -> 137
- net (no net): track 0.00 -> 155.8 mm, vias 0 -> 6
- net /PB0: track 24.8 -> 97.2 mm, vias 0 -> 2
- net /PD3: track 41.5 -> 97.9 mm, vias 0 -> 4
- net /DDR_DQ7: track 20.2 -> 71.0 mm
- net /DDR_DQ1: track 21.3 -> 71.8 mm
- net Net-(J2-Pin_1): track 0.00 -> 48.5 mm, vias 0 -> 2
- net /PE3: track 48.5 -> 0.00 mm, vias 2 -> 0
- net VDD: track 73.3 -> 120.1 mm, vias 7 -> 20
- net /PB10: track 43.2 -> 0.00 mm, vias 2 -> 0
- net /PC7: track 42.9 -> 0.00 mm, vias 4 -> 0
- net VDDA: track 25.5 -> 68.2 mm, vias 1 -> 4
- net /PG9: track 41.8 -> 0.00 mm, vias 2 -> 0
- net Net-(J1-Pin_63): track 0.00 -> 40.6 mm, vias 0 -> 2
- net /DDR_DQ12: track 21.8 -> 62.4 mm, vias 0 -> 1
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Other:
- board text added: "22uF_0603_6.3V"
- board text added: "AP2411SN"
- board text added: "BAT54S"
- board text added: "L2"
- board text added: "LED1"
- board text added: "LED2"
- board text added: "R3"
- board text added: "R63"
- board text added: "R75"
- board text added: "TAR5S33"
- board text added: "U13"
- board text added: "U18"
- board text added: "U20"

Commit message: mp133 devboard DDR routing started
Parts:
- removed the C102 at (254.1, 59.8)
- removed the C103 at (243.6, 65.3)
- removed the C106 at (244.0, 55.9)
- removed the C110 at (142.8, 74.5)
- removed the C111 at (142.8, 76.5)
- removed the C13 at (204.2, 88.8)
- removed the C174 at (142.5, 64.2)
- removed the C175 at (142.5, 65.9)
- removed the C176 at (142.5, 67.6)
- removed the C177 at (142.5, 69.3)
- removed the C182 at (142.5, 71.0)
- removed the C182 at (249.3, 55.0)
- removed the C183 at (142.5, 72.6)
- removed the C184 at (144.7, 64.2)
- removed the C185 at (144.7, 65.9)
- removed the C186 at (144.7, 67.6)
- removed the C187 at (144.7, 69.3)
- removed the C188 at (144.7, 71.0)
- removed the C189 at (144.7, 72.6)
- removed the C190 at (147.0, 64.2)
- removed the C191 at (147.0, 65.9)
- removed the C192 at (147.0, 67.6)
- removed the C192 at (247.6, 56.9)
- removed the C193 at (147.0, 69.3)
- removed the C194 at (147.0, 71.0)
- removed the C195 at (147.0, 72.6)
- removed the C196 at (149.2, 64.2)
- removed the C197 at (149.2, 65.9)
- removed the C198 at (149.2, 67.6)
- removed the C199 at (149.2, 69.3)
- removed the C200 at (149.2, 71.0)
- removed the C201 at (149.2, 72.6)
- removed the C202 at (151.5, 64.2)
- removed the C203 at (151.5, 65.9)
- removed the C204 at (151.5, 67.6)
- removed the C205 at (151.5, 69.3)
- removed the C206 at (151.5, 71.0)
- removed the C207 at (151.5, 72.6)
- removed the C208 at (153.7, 64.2)
- removed the C209 at (153.7, 65.9)
- removed the C211 at (153.7, 67.6)
- removed the C212 at (153.7, 69.3)
- removed the C213 at (153.7, 71.0)
- removed the C215 at (153.7, 72.6)
- removed the C29 at (215.2, 81.0)
- removed the C30 at (253.0, 79.9)
- removed the C31 at (208.9, 84.1)
- removed the C31 at (252.9, 78.9)
- removed the C32 at (212.7, 81.8)
- removed the C33 at (252.4, 81.0)
- removed the C42 at (253.4, 64.2)
- removed the C43 at (243.6, 60.1)
- removed the C72 at (254.6, 81.9)
- removed the C81 at (254.2, 56.8)
- removed the C83 at (242.7, 55.8)
- removed the C84 at (254.6, 79.8)
- removed the C92 at (243.6, 59.1)
- removed the C94 at (251.6, 57.4)
- removed the C98 at (253.9, 66.5)
- removed the C99 at (255.5, 56.9)
- removed the D11 at (256.1, 72.9)
- removed the D26 at (145.8, 78.3)
- removed R30: 10k_0402, 4ms_Resistor:R_0402
- removed the R52 at (204.7, 78.1)
- removed the R59 at (253.4, 63.0)
- removed the R67 at (253.4, 62.0)
- removed the R68 at (249.6, 61.4)
- removed the R69 at (242.8, 73.9)
- removed the R76 at (139.9, 64.3)
- removed the R77 at (139.9, 66.3)
- removed the R78 at (139.9, 68.3)
- removed the R79 at (139.9, 70.3)
- removed the U14 at (248.4, 61.5)
- removed the U2 at (208.8, 81.1)
- removed the X2 at (151.2, 75.1)
- added C182: 1uF_0201_4V, 4ms_Capacitor:C_0201, F.Cu at (175.4, 61.1)
- added C192: 1nF_0201_4V, 4ms_Capacitor:C_0201, F.Cu at (175.4, 62.8)
- added C31: 1uF_0402_25V, 4ms_Capacitor:C_0402, F.Cu at (244.4, 73.6)
- U2: value STM32MP131DAF7 -> STM32MP133DAF
- moved C14 51.7 mm to (164.2, 60.8)
- moved C24 40.5 mm to (174.2, 68.1)
- moved C174 39.5 mm to (206.1, 84.6)
- moved C175 39.5 mm to (206.1, 80.2)
- moved C176 39.5 mm to (206.1, 82.0)
- moved C177 39.5 mm to (206.1, 83.2)
- moved C183 39.5 mm to (207.0, 85.5)
- moved C184 39.5 mm to (207.1, 80.5)
- moved C185 39.5 mm to (207.2, 81.7)
- moved C186 39.5 mm to (207.2, 83.1)
- moved C187 39.5 mm to (207.2, 84.3)
- moved C188 39.5 mm to (208.3, 81.4)
- moved C189 39.5 mm to (208.1, 82.3)
- moved C190 39.5 mm to (208.2, 83.5)
- moved C191 39.5 mm to (208.6, 85.5)
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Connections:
- net /A5 renamed /PB1
- net /A6 renamed /PG13
- net /A8 renamed /PF11
- CON1 pad 10: /PE4 -> /PB9
- U2 pad A15: unconnected-(U2A-PB9-PadA15) -> /PB9
- U2 pad A18: /D18 -> /PC10
- U2 pad A19: /D9 -> /PC12
- U2 pad A20: /D17 -> /PC9
- U2 pad A3: /CODEC_I2C_SDA -> /PE13
- U2 pad A4: /D3 -> /PE12
- U2 pad A6: /D10 -> /PD12
- U2 pad A7: unconnected-(U2B-PG0-PadA7) -> /PG0
- U2 pad AA10: /D5 -> /PC2
- U2 pad AA16: /USB1_DN -> /USB_HS_DM
- U2 pad AA19: unconnected-(U2A-PA10-PadAA19) -> /PA10
- U2 pad AA3: /A3 -> /PA1
- U2 pad AA4: unconnected-(U2B-PF12-PadAA4) -> /PF12
- U2 pad AA6: unconnected-(U2A-PA4-PadAA6) -> /PA4
- U2 pad AA7: /D11 -> /PC5
- U2 pad B1: unconnected-(U2A-PD0-PadB1) -> /PD0
- U2 pad B10: unconnected-(U2B-PG4-PadB10) -> /PG4
- U2 pad B14: unconnected-(U2A-PC6-PadB14) -> /PC6
- U2 pad B15: /D2 -> unconnected-(U2A-PB15-PadB15)
- U2 pad B16: /D12 -> unconnected-(U2A-PB14-PadB16)
- U2 pad B17: unconnected-(U2B-PE3-PadB17) -> /PE3
- U2 pad B18: /D19 -> /PC11
- U2 pad B2: unconnected-(U2B-PE11-PadB2) -> /PE11
- U2 pad B5: /RED_LED -> unconnected-(U2A-PD8-PadB5)
- U2 pad B6: unconnected-(U2B-PE0-PadB6) -> /PE0
- U2 pad B7: /D14 -> unconnected-(U2B-PE9-PadB7)
- U2 pad B9: unconnected-(U2B-PE8-PadB9) -> /PE8
- U2 pad C1: /CODEC_RESET -> unconnected-(U2A-PB6-PadC1)
- U2 pad C10: unconnected-(U2B-PE10-PadC10) -> /PE10
- U2 pad C13: unconnected-(U2A-PC7-PadC13) -> /PC7
- U2 pad C14: /DEBUG2 -> /DEBUG0
- U2 pad C16: /DEBUG3 -> /DEBUG1
- U2 pad C17: unconnected-(U2B-PG6-PadC17) -> /PG6
- U2 pad C18: /D16 -> /PC8
- U2 pad C19: /D4 -> /PD2
- U2 pad C2: /D1 -> /PD3
- U2 pad C4: /D15 -> unconnected-(U2A-PD14-PadC4)
- U2 pad C5: /CODEC_I2C_SCL -> unconnected-(U2A-PD1-PadC5)
- U2 pad C6: unconnected-(U2A-PB7-PadC6) -> /PB7
- U2 pad D1: /D0 -> /PB8
- U2 pad D2: unconnected-(U2A-PD6-PadD2) -> /PD6
- U2 pad D3: /D13 -> /PH12
- U2 pad D6: unconnected-(U2A-PD10-PadD6) -> /PD10
- U2 pad E13: unconnected-(U2A-PB10-PadE13) -> /PB10
- U2 pad F2: unconnected-(U2B-PG9-PadF2) -> /PG9
- U2 pad F3: unconnected-(U2A-PD11-PadF3) -> /PD11
- U2 pad F4: unconnected-(U2A-PA12-PadF4) -> /PA12
- U2 pad G2: unconnected-(U2B-PG10-PadG2) -> /PG10
- U2 pad G3: unconnected-(U2B-PG5-PadG3) -> /PG5
- U2 pad H2: unconnected-(U2B-PE4-PadH2) -> /PE4
- U2 pad H4: unconnected-(U2B-PG15-PadH4) -> /PG15
- U2 pad J2: unconnected-(U2A-PD13-PadJ2) -> /PD13
- U2 pad K3: /SAI_SD_A -> / PH11
- U2 pad N1: /DFU_BOOT -> /PE2
- U2 pad P2: /SAI_MCLK -> /PA8
- U2 pad R1: /SAI_FS -> /PG1
- U2 pad R3: unconnected-(U2B-PH3-PadR3) -> /PH3
- U2 pad T2: unconnected-(U2B-PE6-PadT2) -> /PE6
- U2 pad U10: /D7 -> /PA6
- U2 pad V1: unconnected-(U2A-PD7-PadV1) -> /PD7
- U2 pad V3: unconnected-(U2B-PG2-PadV3) -> /PG2
- U2 pad V6: unconnected-(U2A-PA7-PadV6) -> /PA7
- U2 pad W1: /SAI_SD_B -> /PG3
- U2 pad W10: unconnected-(U2B-PE5-PadW10) -> /DEBUG1
- U2 pad W12: Net-(U2D-USB_RREF) -> /USB_RREF
- U2 pad W2: /SAI_SCK -> /PG12
- U2 pad W4: /A0 -> /PF13
- U2 pad W5: /D8 -> /PC0
- U2 pad W6: /D6 -> /PC3
- U2 pad W8: /A9 -> /PB0
- U2 pad W9: unconnected-(U2A-PA3-PadW9) -> /PA3
- U2 pad Y16: /USB1_DP -> /USB_HS_DP
- U2 pad Y3: /A7 -> /PA0
- U2 pad Y4: /A1 -> /PA2
- U2 pad Y5: unconnected-(U2A-PA5-PadY5) -> /PA5
- U2 pad Y7: /A4 -> /PC4
- U2 pad Y9: /A2 -> /PC1
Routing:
- net GND: track 442.7 -> 152.7 mm, vias 137 -> 39
- net (no net): track 155.8 -> 0.00 mm, vias 6 -> 0
- net /PD3: track 97.9 -> 0.00 mm, vias 4 -> 0
- net VDD_DDR: track 97.7 -> 17.4 mm, vias 54 -> 4
- net /DDR_DQ1: track 71.8 -> 0.00 mm
- net /PB0: track 97.2 -> 25.5 mm, vias 2 -> 0
- net /DDR_DQ7: track 71.0 -> 0.00 mm
- net /DDR_DQ12: track 62.4 -> 0.00 mm, vias 1 -> 0
- net VDD: track 120.1 -> 58.9 mm, vias 20 -> 3
- net VDDA: track 68.2 -> 13.1 mm, vias 4 -> 0
- net /DDR_DQ13: track 53.6 -> 0.00 mm, vias 4 -> 0
- net /PD0: track 0.00 -> 52.0 mm, vias 0 -> 3
- net /DDR_DQ2: track 51.8 -> 0.00 mm
- net /DDR_DQ3: track 49.8 -> 0.00 mm
- net /DDR_DQS0_N: track 49.5 -> 0.00 mm
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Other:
- board text added: "MP133 Devboard v0.3"
- board text removed: "L2"
- board text removed: "MP153 Devboard v0.2"

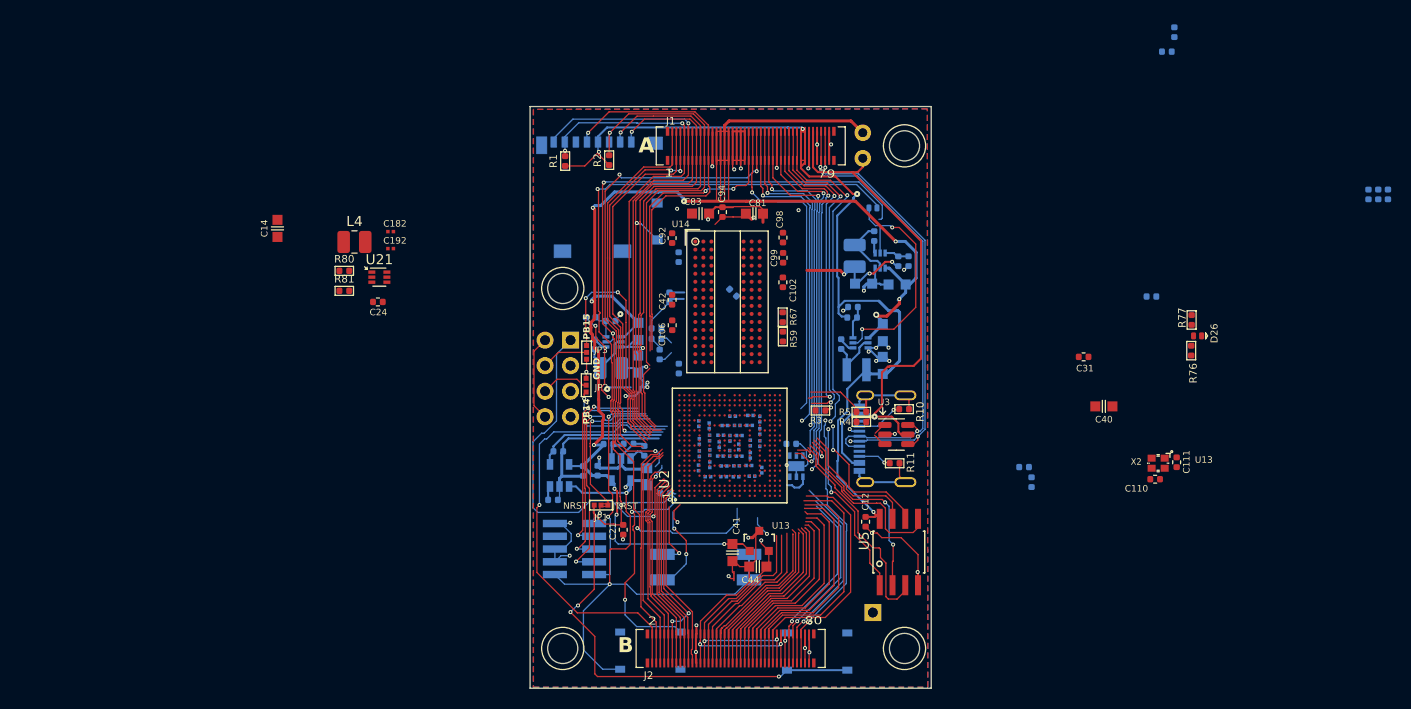
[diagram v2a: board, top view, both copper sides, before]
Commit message: mp133: add DDR pins escaped or has via
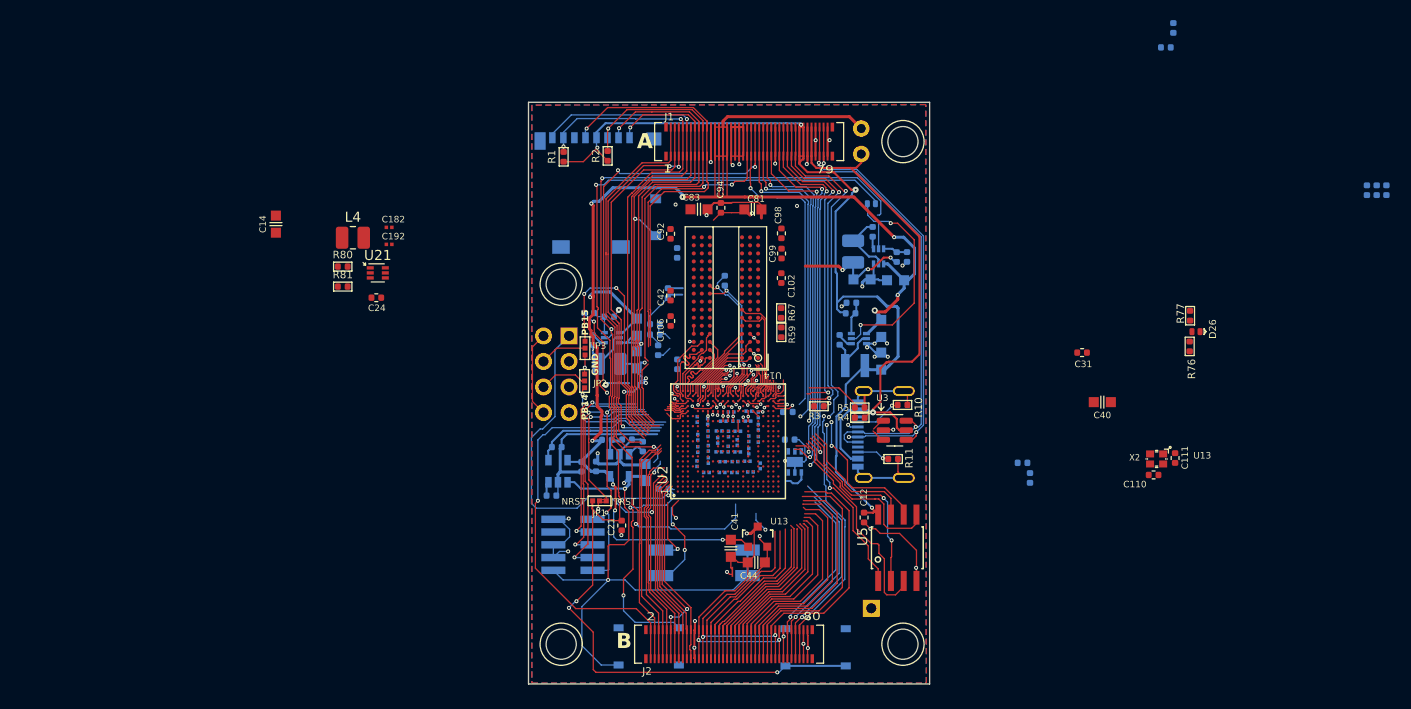
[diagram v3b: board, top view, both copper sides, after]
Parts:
- moved R52 38.0 mm to (214.9, 79.1)
- moved R68 1.45 mm to (208.7, 66.0), turned to 90 degrees
- moved BOOT0_2 0.45 mm to (206.6, 94.1)
- moved C103 0.45 mm to (203.9, 63.3)
- moved C106 0.45 mm to (203.3, 70.0)
- moved C109 0.45 mm to (201.7, 71.4)
- moved C111 0.45 mm to (253.5, 83.7)
- moved C12 0.45 mm to (222.5, 89.6)
- moved C14 0.45 mm to (164.0, 60.4)
- moved C175 0.45 mm to (205.9, 79.8)
- moved C177 0.45 mm to (206.0, 82.8)
- moved C182 0.45 mm to (175.3, 60.7)
- moved C183 0.45 mm to (206.8, 85.1)
- moved C184 0.45 mm to (207.0, 80.0)
- moved C185 0.45 mm to (207.0, 81.2)
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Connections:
- U2 pad B21: /DDR_DQ0 -> /DDR_DQ2
- U2 pad D19: /DDR_DQ2 -> /DDR_DQ0
- U2 pad D20: /DDR_DQ5 -> /DDR_DQ7
- U2 pad F19: /DDR_DQ7 -> /DDR_DQ5
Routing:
- net /DDR_CLK_N: track 0.00 -> 15.0 mm, vias 0 -> 2
- net /DDR_CLK_P: track 0.00 -> 14.2 mm, vias 0 -> 2
- net /DDR_DQS1_P: track 0.00 -> 10.6 mm
- net /DDR_DQS1_N: track 0.00 -> 10.1 mm
- net /DDR_DQ6: track 0.00 -> 8.40 mm
- net VDD_DDR: track 17.4 -> 25.4 mm, vias 4 -> 12
- net /DDR_DQ1: track 0.00 -> 7.91 mm
- net /DDR_DQ4: track 0.00 -> 7.91 mm
- net /DDR_DQM0: track 0.00 -> 7.72 mm
- net /DDR_DQ7: track 0.00 -> 7.63 mm
- net /DDR_DQ5: track 0.00 -> 7.40 mm
- net /DDR_DQ0: track 0.00 -> 7.27 mm
- net /DDR_DQS0_P: track 0.00 -> 7.01 mm
- net /DDR_DQ3: track 0.00 -> 6.96 mm
- net /DDR_DQ2: track 0.00 -> 6.89 mm
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- removed copper zone on In1.Cu, net GND
- removed copper zone on In2.Cu, net GND

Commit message: WIP
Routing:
- net /DDR_DQ13: track 3.14 -> 14.7 mm
- net /DDR_DQ9: track 3.49 -> 13.6 mm
- net /DDR_DQ8: track 3.53 -> 12.6 mm
- net /DDR_DQ10: track 4.01 -> 9.09 mm
- net /DDR_DQ11: track 1.51 -> 4.39 mm
- net /DDR_DQS1_N: track 10.1 -> 12.8 mm
- net VDD_DDR: track 25.4 -> 27.6 mm, vias 12 -> 14
- net /DDR_DQS1_P: track 10.6 -> 12.7 mm
- net GND: track 158.9 -> 161.0 mm, vias 47 -> 49
- net /DDR_DQ14: track 1.11 -> 2.77 mm
- net VREF_DDR: track 8.00 -> 8.46 mm, vias 1 -> 2
